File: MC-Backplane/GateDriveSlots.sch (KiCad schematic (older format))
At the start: 0 parts

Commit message: added reverse polarity protection circuit and fuse
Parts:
- added U? (x3): 86094328314755V1LF, symbol MC-Backplane:86094328314755V1LF
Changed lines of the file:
@@
 $Descr A4 11693 8268
 encoding utf-8
-Sheet 1 5
+Sheet 2 5
 Title ""
 Date ""
@@
 Comment4 ""
 $EndDescr
+$Comp
+L MC-Backplane:86094328314755V1LF U?
+U 1 1 61F26B94
+P 2700 4750
+F 0 "U?" H 2700 6567 50  0000 C CNN
+F 1 "86094328314755V1LF" H 2700 6476 50  0000 C CNN
+F 2 "" H 2700 4750 50  0001 C CNN
+F 3 "" H 2700 4750 50  0001 C CNN
+	1    2700 4750
+	1    0    0    -1
+$EndComp
+$Comp
+L MC-Backplane:86094328314755V1LF U?
+U 1 1 61F29546
+P 5650 4800
+F 0 "U?" H 5650 6617 50  0000 C CNN
+F 1 "86094328314755V1LF" H 5650 6526 50  0000 C CNN
+F 2 "" H 5650 4800 50  0001 C CNN
+F 3 "" H 5650 4800 50  0001 C CNN
+	1    5650 4800
+	1    0    0    -1
+$EndComp
+$Comp
+L MC-Backplane:86094328314755V1LF U?
+U 1 1 61F2AD7B
+P 8400 4750
+F 0 "U?" H 8400 6567 50  0000 C CNN
+F 1 "86094328314755V1LF" H 8400 6476 50  0000 C CNN
+F 2 "" H 8400 4750 50  0001 C CNN
+F 3 "" H 8400 4750 50  0001 C CNN
+	1    8400 4750
+	1    0    0    -1
+$EndComp
 $EndSCHEMATC

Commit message: Add files via upload
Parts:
- removed U? (x2): 86094328314755V1LF, symbol MC-Backplane:86094328314755V1LF
- added U? (x2): 86094328314755V1LF, symbol MC-Backplane:86094328314755V1LF
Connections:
- net GND: now reaches U?.1 (Pin_1)
- net GND: now also U?.10 (Pin_10), U?.11 (Pin_11), U?.12 (Pin_12), U?.13 (Pin_13), U?.14 (Pin_14), U?.18 (Pin_18), U?.2 (Pin_2), U?.20 (Pin_20), U?.22 (Pin_22), U?.24 (Pin_24), U?.26 (Pin_26), U?.28 (Pin_28), U?.3 (Pin_3), U?.30 (Pin_30), U?.32 (Pin_32), U?.4 (Pin_4), U?.5 (Pin_5), U?.6 (Pin_6), U?.7 (Pin_7), U?.8 (Pin_8), U?.9 (Pin_9), U?.1 (Pin_1), U?.1 (Pin_1), U?.10 (Pin_10), U?.10 (Pin_10), U?.11 (Pin_11), U?.11 (Pin_11), U?.12 (Pin_12), U?.12 (Pin_12), U?.13 (Pin_13), U?.13 (Pin_13), U?.14 (Pin_14), U?.14 (Pin_14), U?.18 (Pin_18), U?.18 (Pin_18), U?.2 (Pin_2), U?.2 (Pin_2), U?.20 (Pin_20), U?.20 (Pin_20), U?.22 (Pin_22), U?.22 (Pin_22), U?.24 (Pin_24), U?.24 (Pin_24), U?.26 (Pin_26), U?.26 (Pin_26), U?.28 (Pin_28), U?.28 (Pin_28), U?.3 (Pin_3), U?.3 (Pin_3), U?.30 (Pin_30), U?.30 (Pin_30), U?.32 (Pin_32), U?.32 (Pin_32), U?.4 (Pin_4), U?.4 (Pin_4), U?.5 (Pin_5), U?.5 (Pin_5), U?.6 (Pin_6), U?.6 (Pin_6), U?.7 (Pin_7), U?.7 (Pin_7), U?.8 (Pin_8), U?.8 (Pin_8), U?.9 (Pin_9), U?.9 (Pin_9)
- net 24V: now reaches U?.15 (Pin_15)
- net 24V: now also U?.16 (Pin_16), U?.15 (Pin_15), U?.15 (Pin_15), U?.16 (Pin_16), U?.16 (Pin_16)
- net STATUS1_2: now reaches U?.17 (Pin_17)
- net RESET1_2: now reaches U?.19 (Pin_19)
- net EPWM1_2B: now reaches U?.21 (Pin_21)
- net EPWM1_2A: now reaches U?.23 (Pin_23)
- net STATUS1_1: now reaches U?.25 (Pin_25)
- net RESET1_1: now reaches U?.27 (Pin_27)
- net RESET1_1: now also U?.27 (Pin_27)
- net EPWM1_1B: now reaches U?.29 (Pin_29)
- net EPWM1_1A: now reaches U?.31 (Pin_31)
- new net EPWM2_1A: U?.31 (Pin_31)
- new net EPWM2_1B: U?.29 (Pin_29)
- new net EPWM2_2A: U?.23 (Pin_23)
- new net EPWM2_2B: U?.21 (Pin_21)
- new net EPWM3_1A: U?.31 (Pin_31)
- new net EPWM3_1B: U?.29 (Pin_29)
- new net EPWM3_2A: U?.23 (Pin_23)
- new net EPWM3_2B: U?.21 (Pin_21)
- new net RESET2_1: U?.27 (Pin_27)
- new net RESET2_2: U?.19 (Pin_19)
- new net RESET3_2: U?.19 (Pin_19)
- new net STATUS2_1: U?.25 (Pin_25)
- new net STATUS2_2: U?.17 (Pin_17)
- new net STATUS3_1: U?.25 (Pin_25)
- new net STATUS3_2: U?.17 (Pin_17)
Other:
- note added: "SLOT 1"
- note added: "SLOT 2"
- note added: "SLOT 3"
- moved on the sheet: U?

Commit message: Add files via upload
updating net names and wires
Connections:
- net GND: no longer U?.11 (Pin_11), U?.11 (Pin_11), U?.11 (Pin_11), U?.13 (Pin_13), U?.13 (Pin_13), U?.13 (Pin_13)
- net EPWM1_1A renamed GD_EPWM1_1A
- net EPWM1_1B renamed GD_EPWM1_1B
- net EPWM1_2A renamed GD_EPWM1_2A
- net EPWM1_2B renamed GD_EPWM1_2B
- net EPWM2_1A renamed GD_EPWM2_1A
- net EPWM2_1B renamed GD_EPWM2_1B
- net EPWM2_2A renamed GD_EPWM2_2A
- net EPWM2_2B renamed GD_EPWM2_2B
- net EPWM3_1A renamed GD_EPWM3_1A
- net EPWM3_1B renamed GD_EPWM3_1B
- net EPWM3_2A renamed GD_EPWM3_2A
- net EPWM3_2B renamed GD_EPWM3_2B
- net RESET1_1 renamed GD_RESET1_1
- net RESET1_2 renamed GD_RESET1_2
- net RESET2_1 renamed GD_RESET2_1
- net RESET2_2 renamed GD_RESET2_2
- net RESET3_2 renamed GD_RESET3_2
- net STATUS1_1 renamed GD_DPWM_STATUS1_1
- net STATUS1_2 renamed GD_DPWM_STATUS1_2
- net STATUS2_1 renamed GD_DPWM_STATUS2_1
- net STATUS2_2 renamed GD_DPWM_STATUS2_2
- net STATUS3_1 renamed GD_DPWM_STATUS3_1
- net STATUS3_2 renamed GD_DPWM_STATUS3_2
- new net EMITTER_ENABLE: U?.13 (Pin_13), U?.13 (Pin_13), U?.13 (Pin_13)
- new net SAFE_STATE_FLAG: U?.11 (Pin_11), U?.11 (Pin_11), U?.11 (Pin_11)
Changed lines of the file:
@@
 $Descr A4 11693 8268
 encoding utf-8
-Sheet 5 7
+Sheet 6 7
 Title ""
 Date ""
@@
 	1550 3250 1250 3250
 Wire Wire Line
-	1250 3250 1250 3350
-Wire Wire Line
-	1550 3350 1250 3350
-Connection ~ 1250 3350
-Wire Wire Line
-	1250 3350 1250 3450
-Wire Wire Line
 	1550 3450 1250 3450
 Connection ~ 1250 3450
-Wire Wire Line
-	1250 3450 1250 3550
-Wire Wire Line
-	1550 3550 1250 3550
-Connection ~ 1250 3550
-Wire Wire Line
-	1250 3550 1250 3650
 Wire Wire Line
 	1550 3650 1250 3650
@@
 GND
 Text HLabel 2500 3150 2    50   Input ~ 0
-EPWM1_1A
+GD_EPWM1_1A
 Wire Wire Line
 	2050 4550 2500 4550
@@
 	2050 4350 2500 4350
 Text HLabel 2500 3350 2    50   Input ~ 0
-EPWM1_1B
+GD_EPWM1_1B
 Text HLabel 2500 3550 2    50   Input ~ 0
-RESET1_1
+GD_RESET1_1
 Text HLabel 2500 3750 2    50   Output ~ 0
-STATUS1_1
+GD_DPWM_STATUS1_1
 Text HLabel 2500 3950 2    50   Input ~ 0
-EPWM1_2A
+GD_EPWM1_2A
 Text HLabel 2500 4150 2    50   Input ~ 0
-EPWM1_2B
+GD_EPWM1_2B
 Text HLabel 2500 4350 2    50   Input ~ 0
-RESET1_2
+GD_RESET1_2
 Text HLabel 2500 4550 2    50   Output ~ 0
-STATUS1_2
+GD_DPWM_STATUS1_2
 Text HLabel 1100 3050 0    50   Input ~ 0
 24V
@@
 	4850 3000 4550 3000
 Wire Wire Line
-	4550 3000 4550 3100
-Wire Wire Line
-	4850 3100 4550 3100
-Connection ~ 4550 3100
-Wire Wire Line
-	4550 3100 4550 3200
-Wire Wire Line
 	4850 3200 4550 3200
 Connection ~ 4550 3200
-Wire Wire Line
-	4550 3200 4550 3300
-Wire Wire Line
-	4850 3300 4550 3300
-Connection ~ 4550 3300
-Wire Wire Line
-	4550 3300 4550 3400
 Wire Wire Line
 	4850 3400 4550 3400
@@
 GND
 Text HLabel 5800 2900 2    50   Input ~ 0
-EPWM2_1A
+GD_EPWM2_1A
 Wire Wire Line
 	5350 4300 5800 4300
@@
 	5350 4100 5800 4100
 Text HLabel 5800 3100 2    50   Input ~ 0
-EPWM2_1B
+GD_EPWM2_1B
 Text HLabel 5800 3300 2    50   Input ~ 0
-RESET2_1
+GD_RESET2_1
 Text HLabel 5800 3500 2    50   Output ~ 0
-STATUS2_1
+GD_DPWM_STATUS2_1
 Text HLabel 5800 3700 2    50   Input ~ 0
-EPWM2_2A
+GD_EPWM2_2A
 Text HLabel 5800 3900 2    50   Input ~ 0
-EPWM2_2B
+GD_EPWM2_2B
 Text HLabel 5800 4100 2    50   Input ~ 0
-RESET2_2
+GD_RESET2_2
 Text HLabel 5800 4300 2    50   Output ~ 0
-STATUS2_2
+GD_DPWM_STATUS2_2
 Text HLabel 4400 2800 0    50   Input ~ 0
 24V
@@
 	8600 2950 8300 2950
 Wire Wire Line
-	8300 2950 8300 3050
-Wire Wire Line
-	8600 3050 8300 3050
-Connection ~ 8300 3050
-Wire Wire Line
-	8300 3050 8300 3150
-Wire Wire Line
 	8600 3150 8300 3150
 Connection ~ 8300 3150
-Wire Wire Line
-	8300 3150 8300 3250
-Wire Wire Line
-	8600 3250 8300 3250
-Connection ~ 8300 3250
-Wire Wire Line
-	8300 3250 8300 3350
 Wire Wire Line
 	8600 3350 8300 3350
@@
 GND
 Text HLabel 9550 2850 2    50   Input ~ 0
-EPWM3_1A
+GD_EPWM3_1A
 Wire Wire Line
 	9100 4250 9550 4250
@@
 	9100 4050 9550 4050
 Text HLabel 9550 3050 2    50   Input ~ 0
-EPWM3_1B
+GD_EPWM3_1B
 Text HLabel 9550 3250 2    50   Input ~ 0
-RESET1_1
+GD_RESET1_1
 Text HLabel 9550 3450 2    50   Output ~ 0
-STATUS3_1
+GD_DPWM_STATUS3_1
 Text HLabel 9550 3650 2    50   Input ~ 0
-EPWM3_2A
+GD_EPWM3_2A
 Text HLabel 9550 3850 2    50   Input ~ 0
-EPWM3_2B
+GD_EPWM3_2B
 Text HLabel 9550 4050 2    50   Input ~ 0
-RESET3_2
+GD_RESET3_2
 Text HLabel 9550 4250 2    50   Output ~ 0
-STATUS3_2
+GD_DPWM_STATUS3_2
 Text HLabel 8150 2750 0    50   Input ~ 0
 24V
+Wire Wire Line
+	1250 3250 1250 3450
+Wire Wire Line
+	1250 3450 1250 3650
+Text HLabel 1100 3350 0    50   Input ~ 0
+EMITTER_ENABLE
+Text HLabel 1100 3550 0    50   BiDi ~ 0
+SAFE_STATE_FLAG
+Wire Wire Line
+	1550 3550 1100 3550
+Wire Wire Line
+	1100 3350 1550 3350
+Wire Wire Line
+	4550 3200 4550 3400
+Wire Wire Line
+	4550 3000 4550 3200
+Text HLabel 4400 3300 0    50   BiDi ~ 0
+SAFE_STATE_FLAG
+Text HLabel 4400 3100 0    50   Input ~ 0
+EMITTER_ENABLE
+Text HLabel 8150 3250 0    50   BiDi ~ 0
+SAFE_STATE_FLAG
+Text HLabel 8150 3050 0    50   Input ~ 0
+EMITTER_ENABLE
+Wire Wire Line
+	4850 3100 4400 3100
+Wire Wire Line
+	4400 3300 4850 3300
+Wire Wire Line
+	8300 2950 8300 3150
+Wire Wire Line
+	8300 3150 8300 3350
+Wire Wire Line
+	8150 3050 8600 3050
+Wire Wire Line
+	8600 3250 8150 3250
 $EndSCHEMATC

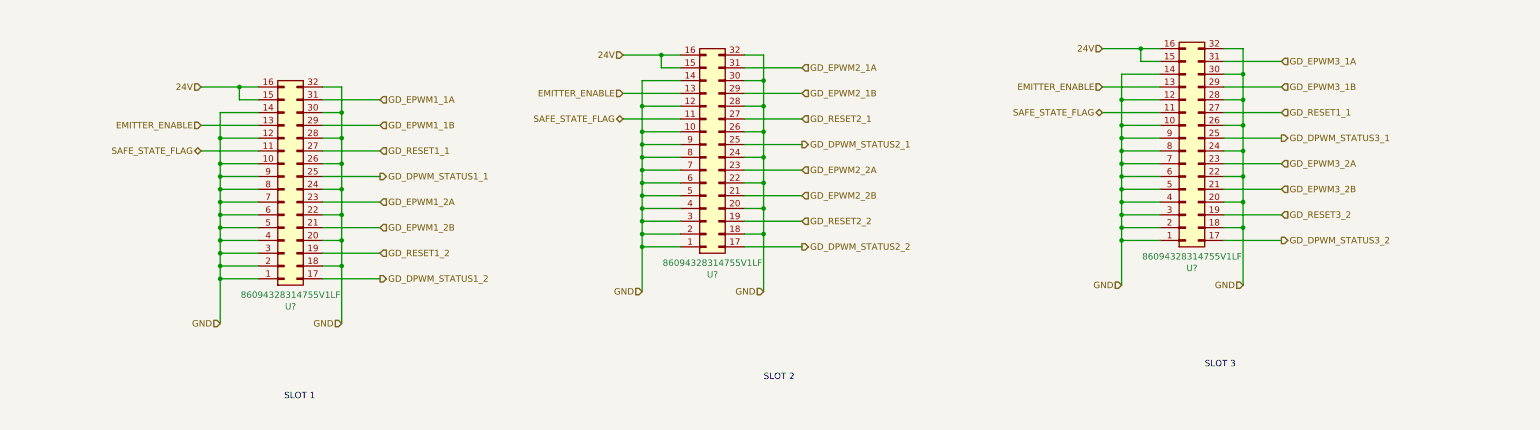
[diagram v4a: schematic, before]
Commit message: Signal naming cleanup/ dsp pin pairing
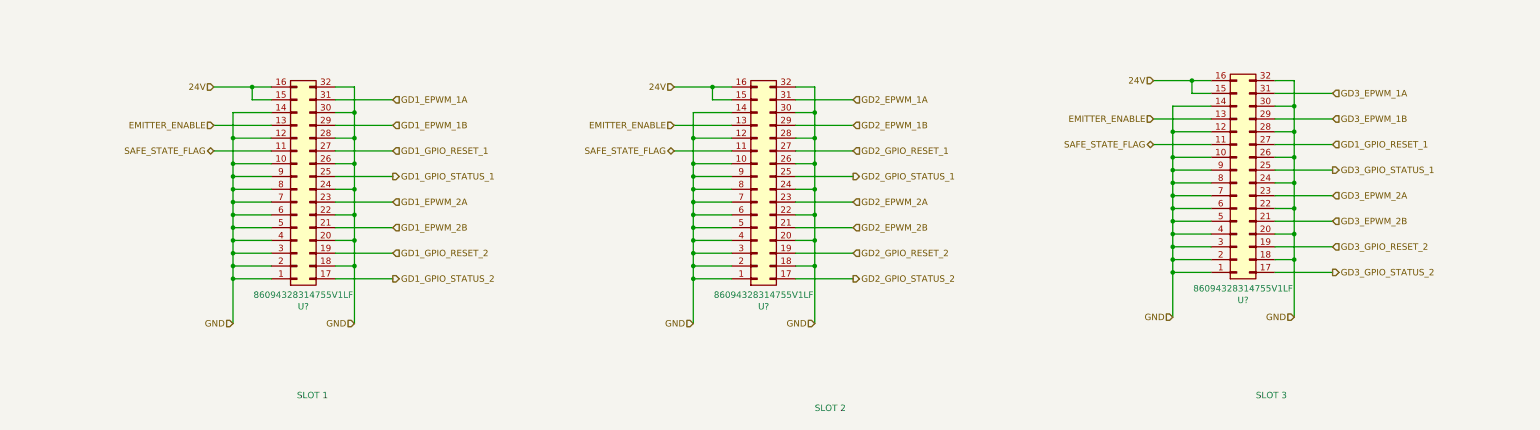
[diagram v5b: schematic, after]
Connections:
- net GD_DPWM_STATUS1_1 renamed GD1_GPIO_STATUS_1
- net GD_DPWM_STATUS1_2 renamed GD1_GPIO_STATUS_2
- net GD_DPWM_STATUS2_1 renamed GD2_GPIO_STATUS_1
- net GD_DPWM_STATUS2_2 renamed GD2_GPIO_STATUS_2
- net GD_DPWM_STATUS3_1 renamed GD3_GPIO_STATUS_1
- net GD_DPWM_STATUS3_2 renamed GD3_GPIO_STATUS_2
- net GD_EPWM1_1A renamed GD1_EPWM_1A
- net GD_EPWM1_1B renamed GD1_EPWM_1B
- net GD_EPWM1_2A renamed GD1_EPWM_2A
- net GD_EPWM1_2B renamed GD1_EPWM_2B
- net GD_EPWM2_1A renamed GD2_EPWM_1A
- net GD_EPWM2_1B renamed GD2_EPWM_1B
- net GD_EPWM2_2A renamed GD2_EPWM_2A
- net GD_EPWM2_2B renamed GD2_EPWM_2B
- net GD_EPWM3_1A renamed GD3_EPWM_1A
- net GD_EPWM3_1B renamed GD3_EPWM_1B
- net GD_EPWM3_2A renamed GD3_EPWM_2A
- net GD_EPWM3_2B renamed GD3_EPWM_2B
- net GD_RESET1_1 renamed GD1_GPIO_RESET_1
- net GD_RESET1_2 renamed GD1_GPIO_RESET_2
- net GD_RESET2_1 renamed GD2_GPIO_RESET_1
- net GD_RESET2_2 renamed GD2_GPIO_RESET_2
- net GD_RESET3_2 renamed GD3_GPIO_RESET_2
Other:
- moved on the sheet: U?

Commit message: DSP interface pin out
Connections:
- net EMITTER_ENABLE is gone; now on net GND: U?.13 (Pin_13), U?.13 (Pin_13), U?.13 (Pin_13)
- net GD2_GPIO_STATUS_2 is gone; now on net CLOCK: U?.17 (Pin_17)
- net GD3_GPIO_RESET_2 is gone; now on net GND: U?.19 (Pin_19)
- net GD3_GPIO_STATUS_2 is gone; now on net CLOCK: U?.17 (Pin_17)
- net SAFE_STATE_FLAG is gone; now on net GND: U?.11 (Pin_11), U?.11 (Pin_11), U?.11 (Pin_11)
- net GND: no longer U?.18 (Pin_18), U?.18 (Pin_18), U?.2 (Pin_2), U?.2 (Pin_2), U?.2 (Pin_2), U?.20 (Pin_20), U?.20 (Pin_20), U?.22 (Pin_22), U?.22 (Pin_22), U?.24 (Pin_24), U?.24 (Pin_24), U?.26 (Pin_26), U?.26 (Pin_26), U?.28 (Pin_28), U?.28 (Pin_28), U?.30 (Pin_30), U?.30 (Pin_30), U?.32 (Pin_32), U?.32 (Pin_32), U?.4 (Pin_4), U?.4 (Pin_4), U?.4 (Pin_4), U?.6 (Pin_6), U?.6 (Pin_6), U?.6 (Pin_6)
- net GD1_EPWM_1A renamed GD1_EPWM_12A
- net GD1_EPWM_1B renamed GD1_EPWM_12B
- net GD1_EPWM_2A renamed GD1_EPWM_11B
- net GD1_EPWM_2B renamed GD1_GPIO52_STATUS_2
- net GD1_GPIO_RESET_1 renamed GD1_GPIO53_STATUS_1
- net GD1_GPIO53_STATUS_1: no longer U?.27 (Pin_27)
- net GD1_GPIO_RESET_2: no longer names the net of U?.19 (Pin_19)
- net GD1_GPIO_RESET_2: now also U?.18 (Pin_18), U?.20 (Pin_20), U?.22 (Pin_22), U?.24 (Pin_24), U?.26 (Pin_26), U?.28 (Pin_28), U?.30 (Pin_30), U?.32 (Pin_32)
- net GD1_GPIO_STATUS_1 renamed GD1_EPWM_11A
- net GD1_GPIO_STATUS_2 renamed CLOCK
- net GD2_EPWM_1A renamed GD2_EPWM_10A
- net GD2_EPWM_1B renamed GD2_EPWM_10B
- net GD2_EPWM_2A renamed GD2_EPWM_9B
- net GD2_EPWM_2B renamed GD2_GPIO44_STATUS_2
- net GD2_GPIO_RESET_1 renamed GD2_GPIO45_STATUS_1
- net GD2_GPIO_RESET_2: no longer names the net of U?.19 (Pin_19)
- net GD2_GPIO_RESET_2: now also U?.18 (Pin_18), U?.20 (Pin_20), U?.22 (Pin_22), U?.24 (Pin_24), U?.26 (Pin_26), U?.28 (Pin_28), U?.30 (Pin_30), U?.32 (Pin_32)
- net GD2_GPIO_STATUS_1 renamed GD2_EPWM_9A
- net GD3_EPWM_1A renamed GD3_EPWM_8A
- net GD3_EPWM_1B renamed GD3_EPWM_8B
- net GD3_EPWM_2A renamed GD3_EPWM_7B
- net GD3_EPWM_2B renamed GD3_GPIO24_STATUS_2
- net GD3_GPIO_STATUS_1 renamed GD3_EPWM_7A
- new net GD3_GPIO25_STATUS_1: U?.27 (Pin_27)
- new net GD_GPIO14_RESET: U?.6 (Pin_6), U?.6 (Pin_6), U?.6 (Pin_6)
- new net GPIO12_EMITTER_ENABLE: U?.4 (Pin_4), U?.4 (Pin_4), U?.4 (Pin_4)
- new net GPIO13_SAFE_STATE_FLAG: U?.2 (Pin_2), U?.2 (Pin_2), U?.2 (Pin_2)

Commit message: beginning layout
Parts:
- removed U? (x2): 86094328314755V1LF, symbol MC-Backplane:86094328314755V1LF
- added U12, U13: 86094328314755V1LF, Footprints_MC-Backplane:86094328314755V1LF, symbol Existing_IC_Models:86094328314755V1LF
- U11: renamed from U?; footprint (none) -> Footprints_MC-Backplane:86094328314755V1LF; symbol MC-Backplane:86094328314755V1LF -> Existing_IC_Models:86094328314755V1LF
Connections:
- net 24V: now also U11.A1, U11.A2, U12.A1, U12.A2, U13.A1, U13.A2; no longer U11.15 (Pin_15), U11.16 (Pin_16)
- net CLOCK: now also U11.C16, U12.C16, U13.C16; no longer U11.17 (Pin_17)
- net GD1_EPWM_11A: now also U11.C8; no longer U11.25 (Pin_25)
- net GD1_EPWM_11B: now also U11.C10; no longer U11.23 (Pin_23)
- net GD1_EPWM_12A: now also U11.C2; no longer U11.31 (Pin_31)
- net GD1_EPWM_12B: now also U11.C4; no longer U11.29 (Pin_29)
- net GD1_GPIO52_STATUS_2: now also U11.C12; no longer U11.21 (Pin_21)
- net GD1_GPIO53_STATUS_1: now also U11.C6; no longer U11.27 (Pin_27)
- net GD2_EPWM_10A: now also U12.C2
- net GD2_EPWM_10B: now also U12.C4
- net GD2_EPWM_9A: now also U12.C8
- net GD2_EPWM_9B: now also U12.C10
- net GD2_GPIO44_STATUS_2: now also U12.C12
- net GD2_GPIO45_STATUS_1: now also U12.C6
- net GD3_EPWM_7A: now also U13.C8
- net GD3_EPWM_7B: now also U13.C10
- net GD3_EPWM_8A: now also U13.C2
- net GD3_EPWM_8B: now also U13.C4
- net GD3_GPIO24_STATUS_2: now also U13.C12
- net GD3_GPIO25_STATUS_1: now also U13.C6
- net GD_GPIO14_RESET: now also U11.A11, U12.A11, U13.A11; no longer U11.6 (Pin_6)
- net GND: now also U11.A10, U11.A12, U11.A14, U11.A16, U11.A3, U11.A4, U11.A5, U11.A6, U11.A7, U11.A8, U11.A9, U11.B1, U11.B2, U11.B3, U11.B4, U11.B5, U11.B6, U11.B7, U11.B8, U11.B9, U12.A10, U12.A12, U12.A14, U12.A16, U12.A3, U12.A4, U12.A5, U12.A6, U12.A7, U12.A8, U12.A9, U12.B1, U12.B10, U12.B11, U12.B12, U12.B13, U12.B14, U12.B15, U12.B16, U12.B2, U12.B3, U12.B4, U12.B5, U12.B6, U12.B7, U12.B8, U12.B9, U12.C1, U12.C11, U12.C13, U12.C14, U12.C15, U12.C3, U12.C5, U12.C7, U12.C9, U13.A10, U13.A12, U13.A14, U13.A16, U13.A3, U13.A4, U13.A5, U13.A6, U13.A7, U13.A8, U13.A9, U13.B1, U13.B10, U13.B11, U13.B12, U13.B13, U13.B14, U13.B15, U13.B16, U13.B2, U13.B3, U13.B4, U13.B5, U13.B6, U13.B7, U13.B8, U13.B9, U13.C1, U13.C11, U13.C13, U13.C14, U13.C15, U13.C3, U13.C5, U13.C7, U13.C9; no longer U11.1 (Pin_1), U11.10 (Pin_10), U11.11 (Pin_11), U11.12 (Pin_12), U11.13 (Pin_13), U11.14 (Pin_14), U11.3 (Pin_3), U11.5 (Pin_5), U11.7 (Pin_7), U11.8 (Pin_8), U11.9 (Pin_9)
- net GPIO12_EMITTER_ENABLE: now also U11.A13, U12.A13, U13.A13; no longer U11.4 (Pin_4)
- net GPIO13_SAFE_STATE_FLAG: now also U11.A15, U12.A15, U13.A15; no longer U11.2 (Pin_2)
- new net: U11.B10, U11.B11, U11.B12, U11.B13, U11.B14, U11.B15, U11.B16, U11.C1, U11.C11, U11.C13, U11.C14, U11.C15, U11.C3, U11.C5, U11.C7, U11.C9

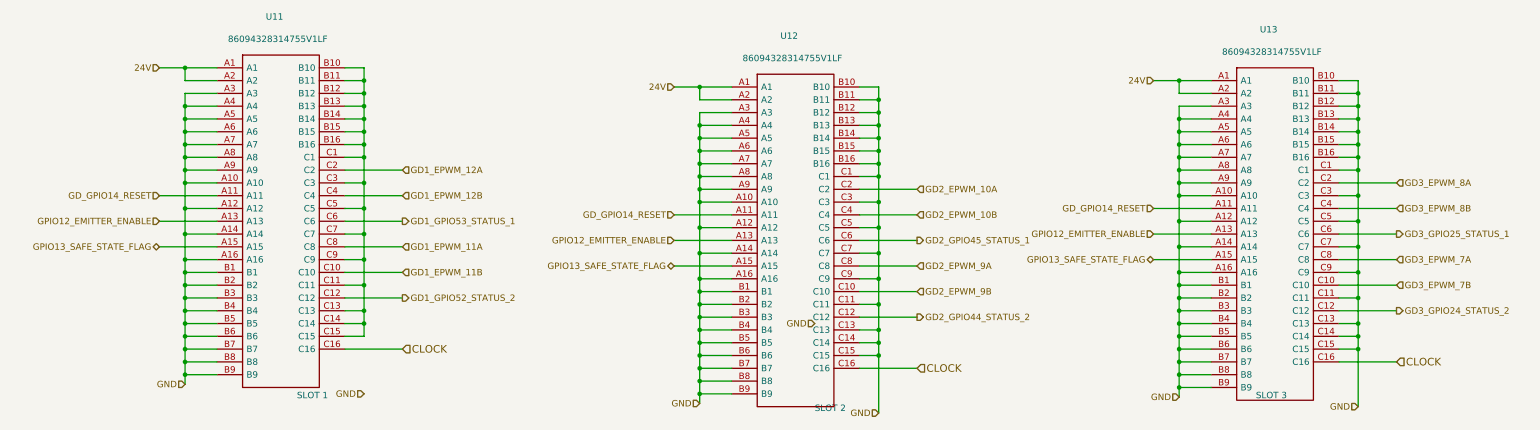
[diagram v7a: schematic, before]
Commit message: schematic reorg and layout begins
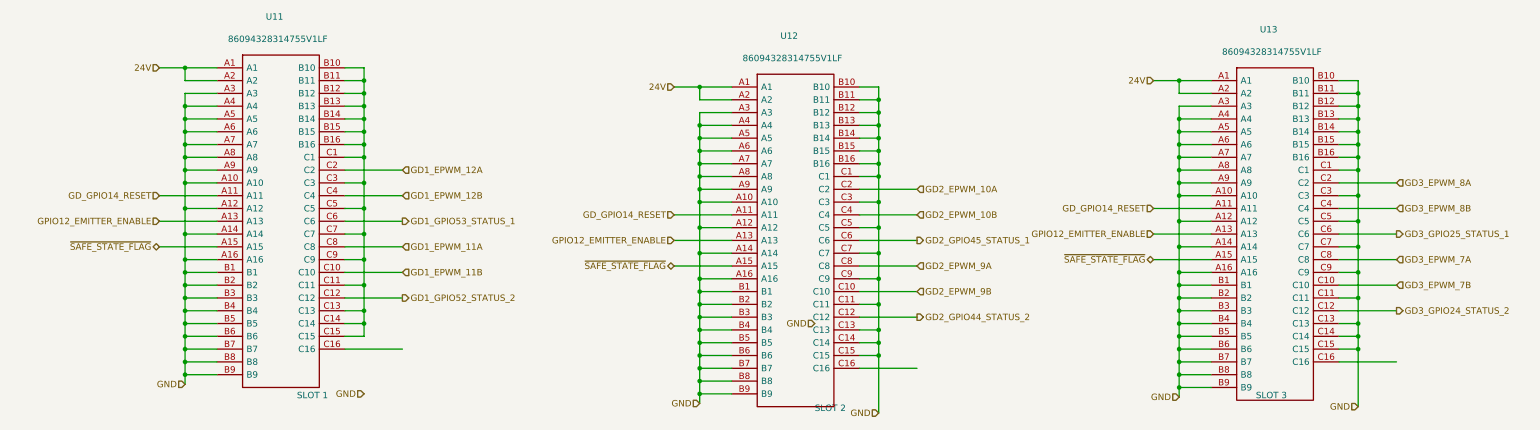
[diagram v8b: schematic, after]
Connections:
- net CLOCK: no longer names the net of U11.C16, U12.C16, U13.C16
- net GPIO13_SAFE_STATE_FLAG renamed ~SAFE_STATE_FLAG~
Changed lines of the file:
@@
 $Descr A4 11693 8268
 encoding utf-8
-Sheet 4 7
+Sheet 4 19
 Title ""
 Date ""
@@
 GPIO12_EMITTER_ENABLE
 Text HLabel 775  4300 0    50   BiDi ~ 0
-GPIO13_SAFE_STATE_FLAG
+~SAFE_STATE_FLAG~
 Wire Wire Line
 	1225 4300 775  4300
@@
 GPIO12_EMITTER_ENABLE
 Text HLabel 4800 4450 0    50   BiDi ~ 0
-GPIO13_SAFE_STATE_FLAG
+~SAFE_STATE_FLAG~
 Wire Wire Line
 	9000 4400 8550 4400
@@
 GPIO12_EMITTER_ENABLE
 Text HLabel 8550 4400 0    50   BiDi ~ 0
-GPIO13_SAFE_STATE_FLAG
+~SAFE_STATE_FLAG~
 Text HLabel 6700 4250 2    50   Output ~ 0
 GD2_GPIO45_STATUS_1
@@
 	2225 5100 2675 5100
 Text HLabel 2675 5100 2    59   Input ~ 0
-CLOCK
 Text HLabel 6700 5250 2    59   Input ~ 0
-CLOCK
 Text HLabel 10450 5200 2    59   Input ~ 0
-CLOCK
 Wire Wire Line
 	1225 4500 975  4500
